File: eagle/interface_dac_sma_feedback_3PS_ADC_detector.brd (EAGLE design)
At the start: 112.9 x 165 mm, 38 parts, among them IC1 ISO1540, IC2 LT1352PA, IC3 LT1352PA, X1 BU-SMA-V

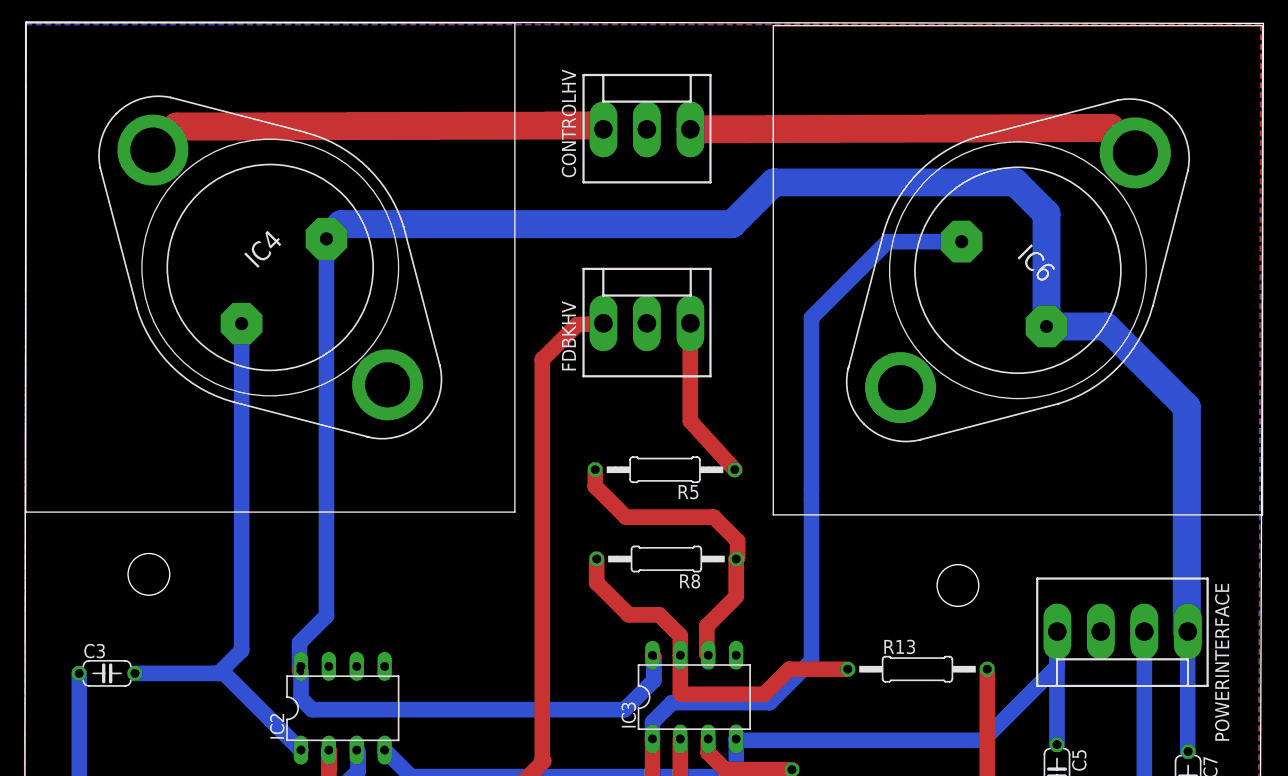
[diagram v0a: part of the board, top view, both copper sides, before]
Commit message: update for thermal issues and CTIA breakout
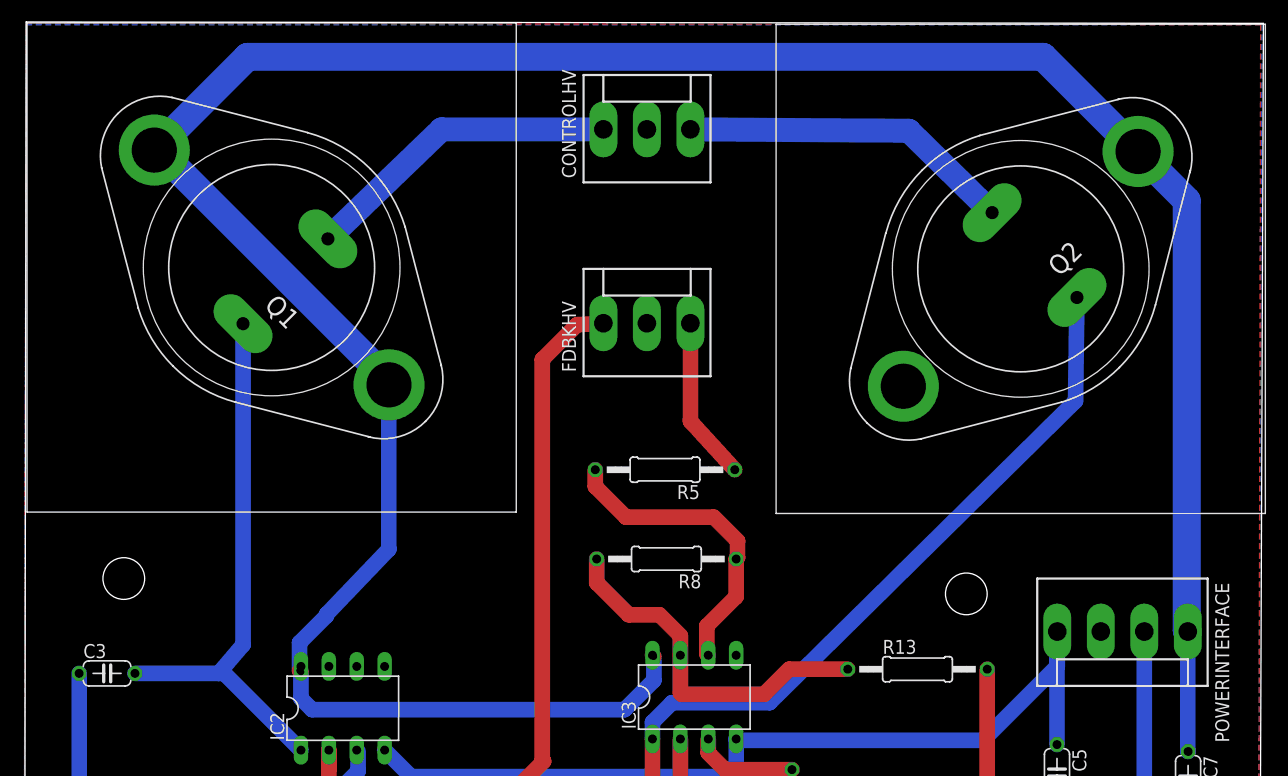
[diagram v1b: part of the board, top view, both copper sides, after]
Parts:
- removed IC4, IC6: (no value), v-reg:TO3-K02
- added Q1, Q2: 2N3055, transistor-npn:TO3
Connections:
- net +15V: now also Q1.C, Q1.C/, Q2.C, Q2.C/; no longer IC4.1, IC6.1
- net N$19: now also Q1.B; no longer IC4.2
- net N$21: now also Q2.B; no longer IC6.2
- net N$4: now also Q1.E; no longer IC4.3
- net N$5: now also Q2.E; no longer IC6.3
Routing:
- net +15V: track 205.3 -> 251.5 mm
- net N$4: track 42.2 -> 29.1 mm
- net N$5: track 41.4 -> 30.5 mm
- net N$21: track 72.4 -> 67.8 mm
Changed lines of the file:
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@@
 <hole x="93.599" y="6.35" drill="3.7973"/>
 <hole x="16.383" y="6.35" drill="3.7973"/>
-<hole x="11.43" y="114.554" drill="3.7973"/>
-<hole x="85.09" y="113.538" drill="3.7973"/>
+<hole x="9.144" y="114.173" drill="3.7973"/>
+<hole x="85.852" y="112.776" drill="3.7973"/>
 </plain>
 <attributes>
@@
 </element>
 <element name="R13" library="resistor" package="0207/12" value="10k" x="81.407" y="105.918"/>
-<element name="IC4" library="v-reg" package="TO3-K02" value="" x="22.479" y="142.494" rot="R135"/>
-<element name="IC6" library="v-reg" package="TO3-K02" value="" x="90.551" y="142.24" rot="R45"/>
 <element name="U$3" library="texas" package="DIL10" value="ADS1015DIL" x="51.181" y="82.55" rot="R180"/>
 <element name="R14" library="rcl" package="0207/12" value="100" x="12.446" y="27.686" rot="R270"/>
@@
 <attribute name="OC_FARNELL" value="unknown" x="12.192" y="77.851" size="1.778" layer="27" display="off"/>
 </element>
+<element name="Q1" library="transistor-npn" package="TO3" value="2N3055" x="22.606" y="142.494" rot="R135"/>
+<element name="Q2" library="transistor-npn" package="TO3" value="2N3055" x="90.805" y="142.367" rot="R225"/>
 </elements>
 <signals>
@@
 <contactref element="IC2" pad="1"/>
 <wire x1="18.288" y1="105.537" x2="25.273" y2="98.552" width="1.4224" layer="16"/>
-<contactref element="IC4" pad="2"/>
 <wire x1="18.288" y1="105.537" x2="18.288" y2="105.664" width="1.4224" layer="16"/>
 <wire x1="10.16" y1="105.537" x2="17.78" y2="105.537" width="1.4224" layer="16"/>
 <wire x1="17.78" y1="105.537" x2="18.161" y2="105.537" width="1.4224" layer="16"/>
 <wire x1="18.161" y1="105.537" x2="18.288" y2="105.664" width="1.4224" layer="16"/>
-<wire x1="19.874725" y1="137.375253125" x2="19.874725" y2="107.631725" width="1.4224" layer="16"/>
-<wire x1="19.874725" y1="107.631725" x2="17.78" y2="105.537" width="1.4224" layer="16"/>
+<wire x1="20.001725" y1="108.139725" x2="17.78" y2="105.537" width="1.4224" layer="16"/>
+<contactref element="Q1" pad="B"/>
+<wire x1="20.001725" y1="137.375253125" x2="20.001725" y2="108.139725" width="1.4224" layer="16"/>
 </signal>
 <signal name="N$22">
@@
 <wire x1="57.277" y1="99.568" x2="57.277" y2="93.599" width="1.4224" layer="1"/>
 <wire x1="57.277" y1="93.599" x2="57.023" y2="93.345" width="1.4224" layer="1"/>
-<contactref element="IC6" pad="2"/>
-<wire x1="71.755" y1="122.301" x2="71.755" y2="121.412" width="1.4224" layer="16"/>
-<wire x1="71.755" y1="121.412" x2="71.755" y2="106.68" width="1.4224" layer="16"/>
-<wire x1="71.755" y1="106.68" x2="67.945" y2="102.87" width="1.4224" layer="16"/>
 <wire x1="67.945" y1="102.87" x2="59.055" y2="102.87" width="1.4224" layer="16"/>
 <wire x1="59.055" y1="102.87" x2="57.277" y2="101.092" width="1.4224" layer="16"/>
 <wire x1="57.277" y1="101.092" x2="57.277" y2="99.568" width="1.4224" layer="16"/>
-<wire x1="85.432253125" y1="144.844271875" x2="78.677271875" y2="144.844271875" width="1.4224" layer="16"/>
-<wire x1="78.677271875" y1="144.844271875" x2="71.755" y2="137.922" width="1.4224" layer="16"/>
-<wire x1="71.755" y1="137.922" x2="71.755" y2="122.301" width="1.4224" layer="16"/>
+<contactref element="Q2" pad="B"/>
+<wire x1="95.92374375" y1="139.762725" x2="95.79674375" y2="130.34074375" width="1.4224" layer="16"/>
+<wire x1="95.79674375" y1="130.34074375" x2="67.945" y2="102.87" width="1.4224" layer="16"/>
 </signal>
 <signal name="N$3">
@@
 <wire x1="7.366" y1="31.242" x2="7.366" y2="42.037" width="1.4224" layer="16"/>
 </signal>
-<signal name="N$4">
-<contactref element="IC4" pad="3"/>
-<contactref element="CONTROLHV" pad="1"/>
-<wire x1="52.705" y1="155.425" x2="52.809" y2="155.067" width="2.54" layer="1"/>
-<wire x1="52.705" y1="155.425" x2="13.932990625" y2="155.321" width="2.54" layer="1"/>
-<wire x1="13.932990625" y1="155.321" x2="11.79249375" y2="153.180503125" width="2.54" layer="1"/>
-</signal>
-<signal name="N$5">
-<contactref element="IC6" pad="3"/>
-<contactref element="CONTROLHV" pad="3"/>
-<wire x1="60.729" y1="155.067" x2="98.97000625" y2="155.194" width="2.54" layer="1"/>
-<wire x1="98.97000625" y1="155.194" x2="101.237503125" y2="152.926503125" width="2.54" layer="1"/>
-</signal>
 <signal name="N$8">
 <contactref element="R5" pad="1"/>
@@
 <contactref element="IC2" pad="8"/>
 <contactref element="IC3" pad="8"/>
-<contactref element="IC6" pad="1"/>
 <contactref element="C7" pad="1"/>
 <contactref element="POWERINTERFACE" pad="1"/>
-<contactref element="IC4" pad="1"/>
 <wire x1="25.146" y1="108.331" x2="25.146" y2="105.791" width="1.4224" layer="16"/>
 <wire x1="25.146" y1="105.791" x2="25.273" y2="105.664" width="1.4224" layer="1"/>
@@
 <via x="25.146" y="105.791" extent="1-16" drill="0.6" shape="square"/>
 <via x="57.404" y="107.061" extent="1-16" drill="0.6" shape="square"/>
-<wire x1="93.155271875" y1="137.121253125" x2="98.590746875" y2="137.121253125" width="2.54" layer="16"/>
-<wire x1="98.590746875" y1="137.121253125" x2="105.918" y2="129.794" width="2.54" layer="16"/>
-<wire x1="105.918" y1="129.794" x2="105.918" y2="109.445" width="2.54" layer="16"/>
+<wire x1="105.918" y1="148.59" x2="105.918" y2="109.445" width="2.54" layer="16"/>
 <wire x1="105.918" y1="109.445" x2="106.016" y2="109.347" width="2.54" layer="16"/>
 <wire x1="106.016" y1="109.347" x2="106.016" y2="98.454" width="1.4224" layer="16"/>
 <wire x1="106.016" y1="98.454" x2="106.045" y2="98.425" width="1.4224" layer="16"/>
-<wire x1="93.155271875" y1="137.121253125" x2="93.155271875" y2="147.382728125" width="2.54" layer="16"/>
-<wire x1="93.155271875" y1="147.382728125" x2="90.297" y2="150.241" width="2.54" layer="16"/>
-<wire x1="90.297" y1="150.241" x2="68.326" y2="150.241" width="2.54" layer="16"/>
-<wire x1="68.326" y1="150.241" x2="64.516" y2="146.431" width="2.54" layer="16"/>
-<wire x1="64.516" y1="146.431" x2="28.930471875" y2="146.431" width="2.54" layer="16"/>
-<wire x1="28.930471875" y1="146.431" x2="27.59774375" y2="145.098271875" width="2.54" layer="16"/>
-<wire x1="27.59774375" y1="145.098271875" x2="27.59774375" y2="110.78274375" width="1.4224" layer="16"/>
 <wire x1="27.59774375" y1="110.78274375" x2="25.146" y2="108.331" width="1.4224" layer="16"/>
-<wire x1="25.146" y1="105.791" x2="25.273" y2="106.172" width="0" layer="19" extent="16-16"/>
+<contactref element="Q1" pad="C/" route="any" routetag="A.C"/>
+<contactref element="Q1" pad="C" route="any" routetag="A.C"/>
+<contactref element="Q2" pad="C/" route="any" routetag="A.C"/>
+<contactref element="Q2" pad="C" route="any" routetag="A.C"/>
+<wire x1="27.59774375" y1="110.78274375" x2="27.59774375" y2="110.90974375" width="1.4224" layer="16"/>
+<wire x1="27.59774375" y1="110.90974375" x2="33.274" y2="116.84" width="1.4224" layer="16"/>
+<wire x1="105.918" y1="148.59" x2="92.837" y2="161.671" width="2.54" layer="16"/>
+<wire x1="92.837" y1="161.671" x2="20.409990625" y2="161.671" width="2.54" layer="16"/>
+<wire x1="20.409990625" y1="161.671" x2="11.91949375" y2="153.180503125" width="2.54" layer="16"/>
+<wire x1="33.292503125" y1="131.80749375" x2="33.292503125" y2="132.188496875" width="2.54" layer="16"/>
+<wire x1="33.292503125" y1="132.188496875" x2="12.065" y2="153.416" width="2.54" layer="16"/>
+<wire x1="33.274" y1="116.84" x2="33.274" y2="131.788990625" width="1.4224" layer="16"/>
+<wire x1="33.274" y1="131.788990625" x2="33.292503125" y2="131.80749375" width="1.4224" layer="16"/>
+<wire x1="105.918" y1="148.59" x2="101.491503125" y2="153.053503125" width="0" layer="19" extent="16-16"/>
+<wire x1="25.273" y1="106.172" x2="25.146" y2="105.791" width="0" layer="19" extent="16-16"/>
 </signal>
 <signal name="-15V">
@@
 <wire x1="94.107" y1="109.318" x2="94.136" y2="109.347" width="1.4224" layer="16"/>
 </signal>
+<signal name="N$4">
+<contactref element="Q1" pad="E"/>
+<contactref element="CONTROLHV" pad="1"/>
+<wire x1="52.809" y1="155.067" x2="38.074471875" y2="155.067" width="2.1844" layer="16"/>
+<wire x1="38.074471875" y1="155.067" x2="27.72474375" y2="145.098271875" width="2.1844" layer="16"/>
+</signal>
+<signal name="N$5">
+<contactref element="Q2" pad="E"/>
+<contactref element="CONTROLHV" pad="3"/>
+<wire x1="60.729" y1="155.067" x2="80.61946875" y2="154.94" width="2.1844" layer="16"/>
+<wire x1="80.61946875" y1="154.94" x2="88.200725" y2="147.48574375" width="2.1844" layer="16"/>
+</signal>
 </signals>
